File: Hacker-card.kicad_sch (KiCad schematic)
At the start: 0 parts

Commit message: Created the JOURNAL, added the python venv for easyeda2kicad, and added the symbol and footprint for a surface mount resistor
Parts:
- added U1: RP2040, Package_DFN_QFN:QFN-56-1EP_7x7mm_P0.4mm_EP3.2x3.2mm, symbol MCU_RaspberryPi:RP2040
- added U2: TYPE-C 6PIN, easyeda2kicad:USB-C-SMD, symbol easyeda2kicad:TYPE-C6PIN
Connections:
- new net: U1.1 (IOVDD), U1.10 (IOVDD), U1.22 (IOVDD), U1.33 (IOVDD), U1.42 (IOVDD), U1.49 (IOVDD)
- new net: U1.23 (DVDD), U1.50 (DVDD)
- new net GND: U1.57 (GND), U2.A12 (GND), U2.B12 (GND)

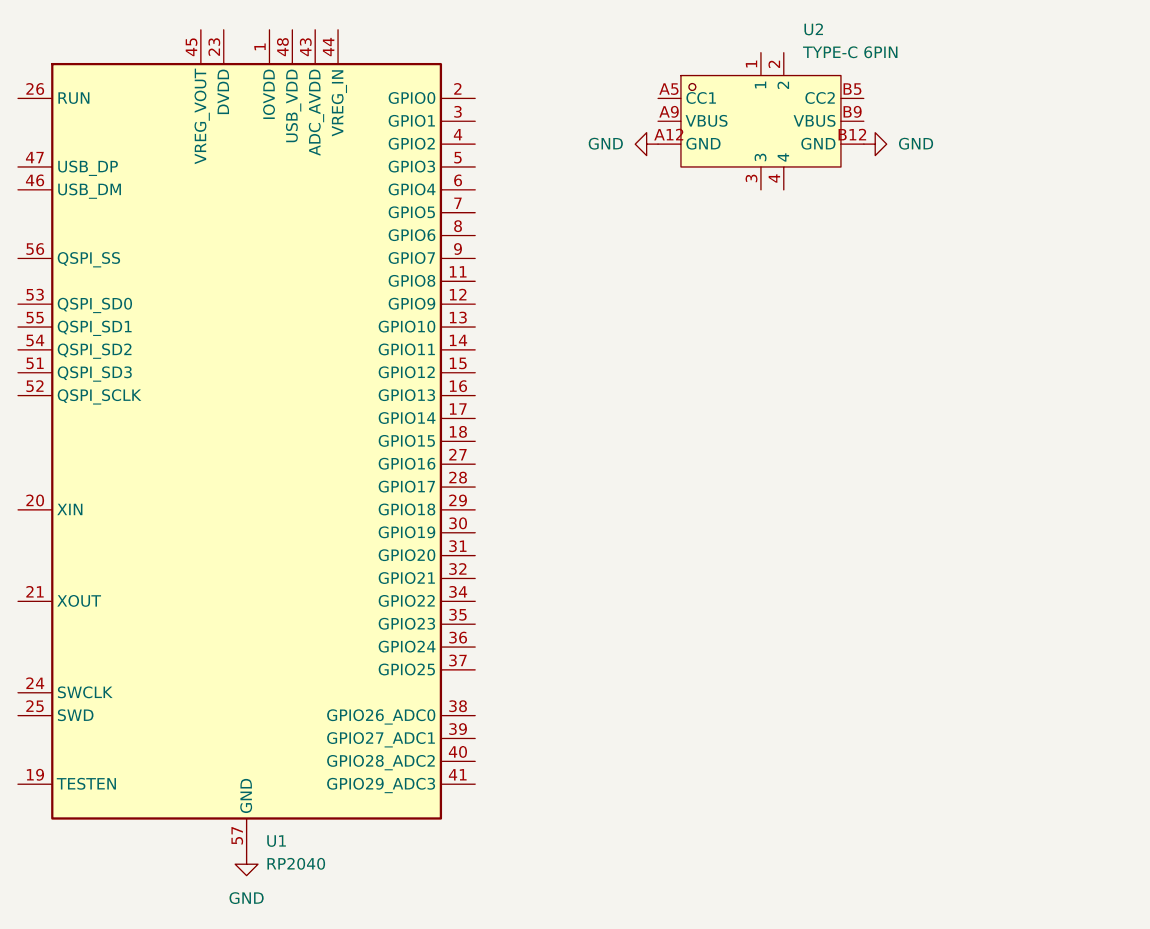
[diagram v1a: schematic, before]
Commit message: Updated the pcb project and gitignore
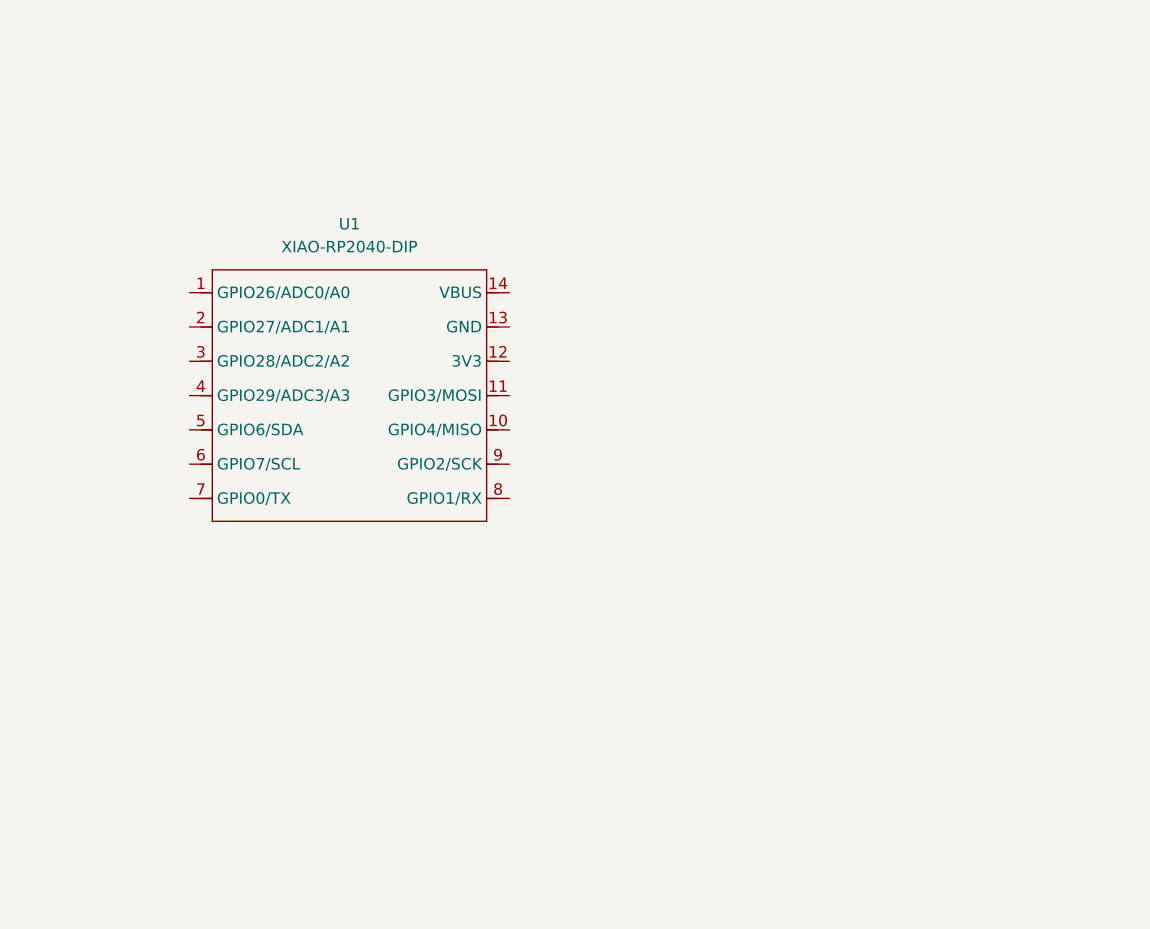
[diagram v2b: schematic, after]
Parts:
- removed U1: RP2040, Package_DFN_QFN:QFN-56-1EP_7x7mm_P0.4mm_EP3.2x3.2mm, symbol MCU_RaspberryPi:RP2040
- removed U2: TYPE-C 6PIN, easyeda2kicad:USB-C-SMD, symbol easyeda2kicad:TYPE-C6PIN
- added U1: XIAO-RP2040-DIP, OPL:XIAO-RP2040-DIP, symbol OPL:XIAO-RP2040-DIP

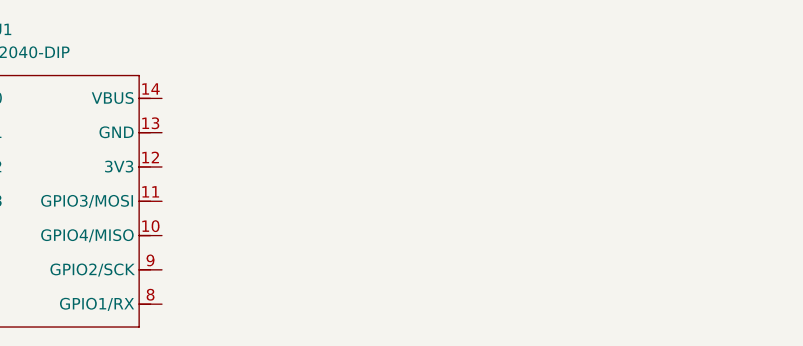
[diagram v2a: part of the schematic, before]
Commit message: Added the MOSI wire in the schematic
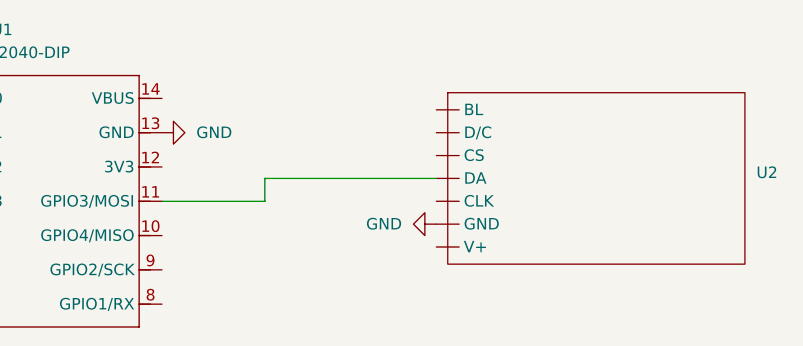
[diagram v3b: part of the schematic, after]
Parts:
- added U2: ~, symbol display:Newxie
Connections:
- net at U1.11 (GPIO3/MOSI): now also U2. (V+)
- net GND: now reaches U1.13 (GND)
- net GND: now also U2. (V+)
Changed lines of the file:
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@@
 	(generator_version "9.0")
 	(paper "A4")
+	(wire
+		(pts
+			(xy 106.68 86.36) (xy 125.73 86.36)
+		)
+		(stroke
+			(width 0)
+			(type default)
+		)
+	)
+	(wire
+		(pts
+			(xy 106.68 88.9) (xy 106.68 86.36)
+		)
+		(stroke
+			(width 0)
+			(type default)
+		)
+	)
+	(wire
+		(pts
+			(xy 95.25 88.9) (xy 106.68 88.9)
+		)
+		(stroke
+			(width 0)
+			(type default)
+		)
+	)
+	(symbol
+		(lib_id "power:GND")
+		(at 95.25 81.28 90)
+		(unit 1)
+		(exclude_from_sim no)
+		(in_bom yes)
+		(on_board yes)
+		(dnp no)
+		(fields_autoplaced yes)
+		(property "Reference" "#PWR02"
+			(at 101.6 81.28 0)
+			(effects
+				(font
+					(size 1.27 1.27)
+				)
+				(hide yes)
+			)
+		)
+		(property "Value" "GND"
+			(at 99.06 81.2799 90)
+			(effects
+				(font
+					(size 1.27 1.27)
+				)
+				(justify right)
+			)
+		)
+		(property "Footprint" ""
+			(at 95.25 81.28 0)
+			(effects
+				(font
+					(size 1.27 1.27)
+				)
+				(hide yes)
+			)
+		)
+		(property "Datasheet" ""
+			(at 95.25 81.28 0)
+			(effects
+				(font
+					(size 1.27 1.27)
+				)
+				(hide yes)
+			)
+		)
+		(property "Description" "Power symbol creates a global label with name \"GND\" , ground"
+			(at 95.25 81.28 0)
+			(effects
+				(font
+					(size 1.27 1.27)
+				)
+				(hide yes)
+			)
+		)
+		(pin "1"
+		)
+		(instances
+			(project ""
+				(path "/dd5d80f8-a2ab-4791-9385-fee7c1d43bf7"
+					(reference "#PWR02")
+					(unit 1)
+				)
+			)
+		)
+	)
+	(symbol
+		(lib_id "display:Newxie")
+		(at 146.05 87.63 0)
+		(unit 1)
+		(exclude_from_sim no)
+		(in_bom yes)
+		(on_board yes)
+		(dnp no)
+		(fields_autoplaced yes)
+		(property "Reference" "U2"
+			(at 161.29 85.7249 0)
+			(effects
+				(font
+					(size 1.27 1.27)
+				)
+				(justify left)
+			)
+		)
+		(property "Value" "~"
+			(at 161.29 87.63 0)
+			(effects
+				(font
+					(size 1.27 1.27)
+				)
+				(justify left)
+			)
+		)
+		(property "Footprint" ""
+			(at 146.05 87.63 0)
+			(effects
+				(font
+					(size 1.27 1.27)
+				)
+				(hide yes)
+			)
+		)
+		(property "Datasheet" ""
+			(at 146.05 87.63 0)
+			(effects
+				(font
+					(size 1.27 1.27)
+				)
+				(hide yes)
+			)
+		)
+		(property "Description" ""
+			(at 146.05 87.63 0)
+			(effects
+				(font
+					(size 1.27 1.27)
+				)
+				(hide yes)
+			)
+		)
+		(pin ""
+		)
+		(pin ""
+		)
+		(pin ""
+		)
+		(pin ""
+		)
+		(pin ""
+		)
+		(pin ""
+		)
+		(pin ""
+		)
+		(instances
+			(project ""
+				(path "/dd5d80f8-a2ab-4791-9385-fee7c1d43bf7"
+					(reference "U2")
+					(unit 1)
+				)
+			)
+		)
+	)
+	(symbol
+		(lib_id "power:GND")
+		(at 125.73 91.44 270)
+		(unit 1)
+		(exclude_from_sim no)
+		(in_bom yes)
+		(on_board yes)
+		(dnp no)
+		(fields_autoplaced yes)
+		(property "Reference" "#PWR01"
+			(at 119.38 91.44 0)
+			(effects
+				(font
+					(size 1.27 1.27)
+				)
+				(hide yes)
+			)
+		)
+		(property "Value" "GND"
+			(at 121.92 91.4399 90)
+			(effects
+				(font
+					(size 1.27 1.27)
+				)
+				(justify right)
+			)
+		)
+		(property "Footprint" ""
+			(at 125.73 91.44 0)
+			(effects
+				(font
+					(size 1.27 1.27)
+				)
+				(hide yes)
+			)
+		)
+		(property "Datasheet" ""
+			(at 125.73 91.44 0)
+			(effects
+				(font
+					(size 1.27 1.27)
+				)
+				(hide yes)
+			)
+		)
+		(property "Description" "Power symbol creates a global label with name \"GND\" , ground"
+			(at 125.73 91.44 0)
+			(effects
+				(font
+					(size 1.27 1.27)
+				)
+				(hide yes)
+			)
+		)
+		(pin "1"
+		)
+		(instances
+			(project ""
+				(path "/dd5d80f8-a2ab-4791-9385-fee7c1d43bf7"
+					(reference "#PWR01")
+					(unit 1)
+				)
+			)
+		)
+	)
 	(symbol
 		(lib_id "OPL:XIAO-RP2040-DIP")
